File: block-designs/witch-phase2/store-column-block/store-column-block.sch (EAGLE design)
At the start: 12 parts, among them IC1 74HC125D

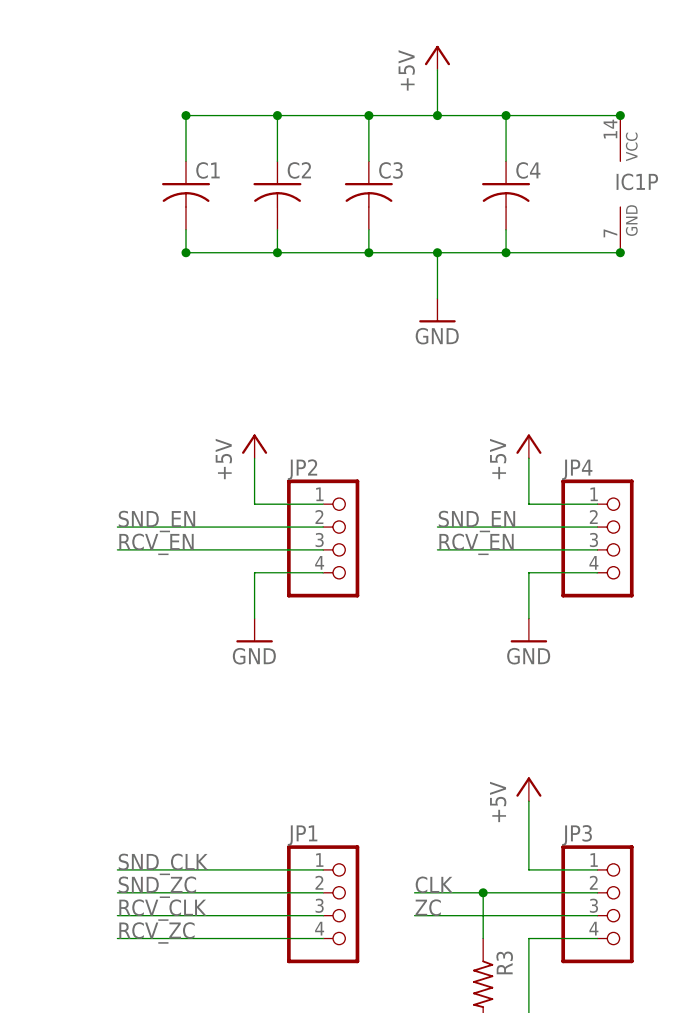
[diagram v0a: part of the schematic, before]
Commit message: updated designs for new labeling and spacing
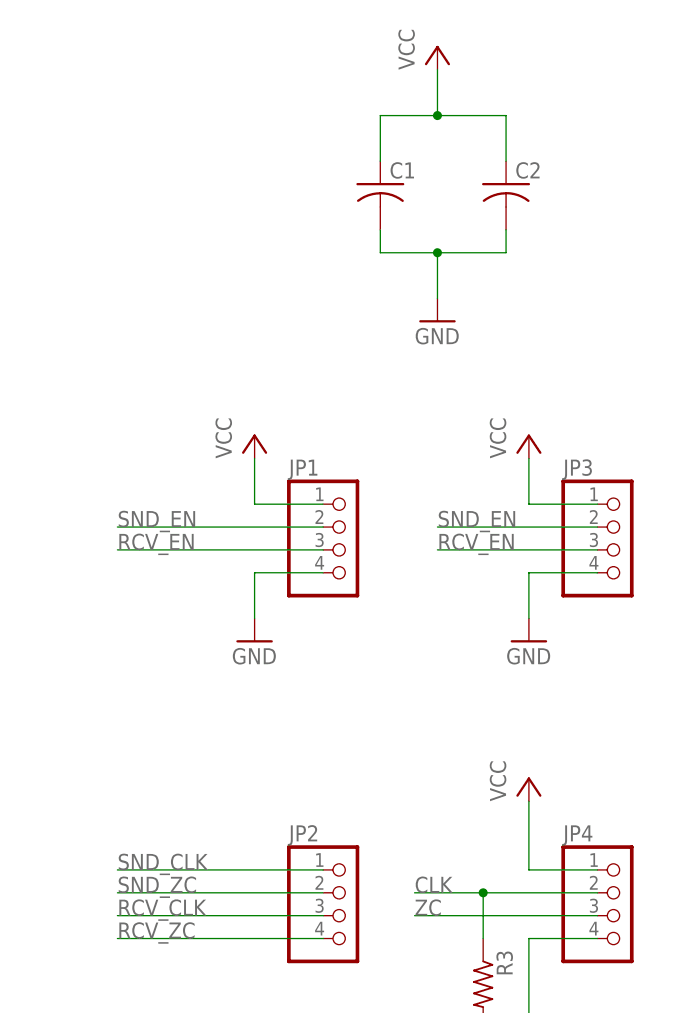
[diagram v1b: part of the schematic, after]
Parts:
- removed C3, C4: (no value), resistor:C-USC0805
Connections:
- removed net +5V: C1.1, C2.1, C3.1, C4.1, IC1P.VCC, JP2.1, JP3.1, JP4.1
- new net VCC: C1.1, C2.1, JP1.1, JP3.1, JP4.1
- net CLK: now also JP4.2; no longer JP3.2
- net GND: now also JP1.4; no longer C3.2, C4.2, IC1P.GND, JP2.4
- net RCV_CLK: now also JP2.3; no longer JP1.3
- net RCV_EN: now also JP1.3, JP3.3; no longer JP2.3, JP4.3
- net RCV_ZC: now also JP2.4; no longer JP1.4
- net SND_CLK: now also JP2.1; no longer JP1.1
- net SND_EN: now also JP1.2, JP3.2; no longer JP2.2, JP4.2
- net SND_ZC: now also JP2.2; no longer JP1.2
- net ZC: now also JP4.3; no longer JP3.3
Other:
- moved on the sheet: C1, C2, JP1, JP2, JP3, JP4

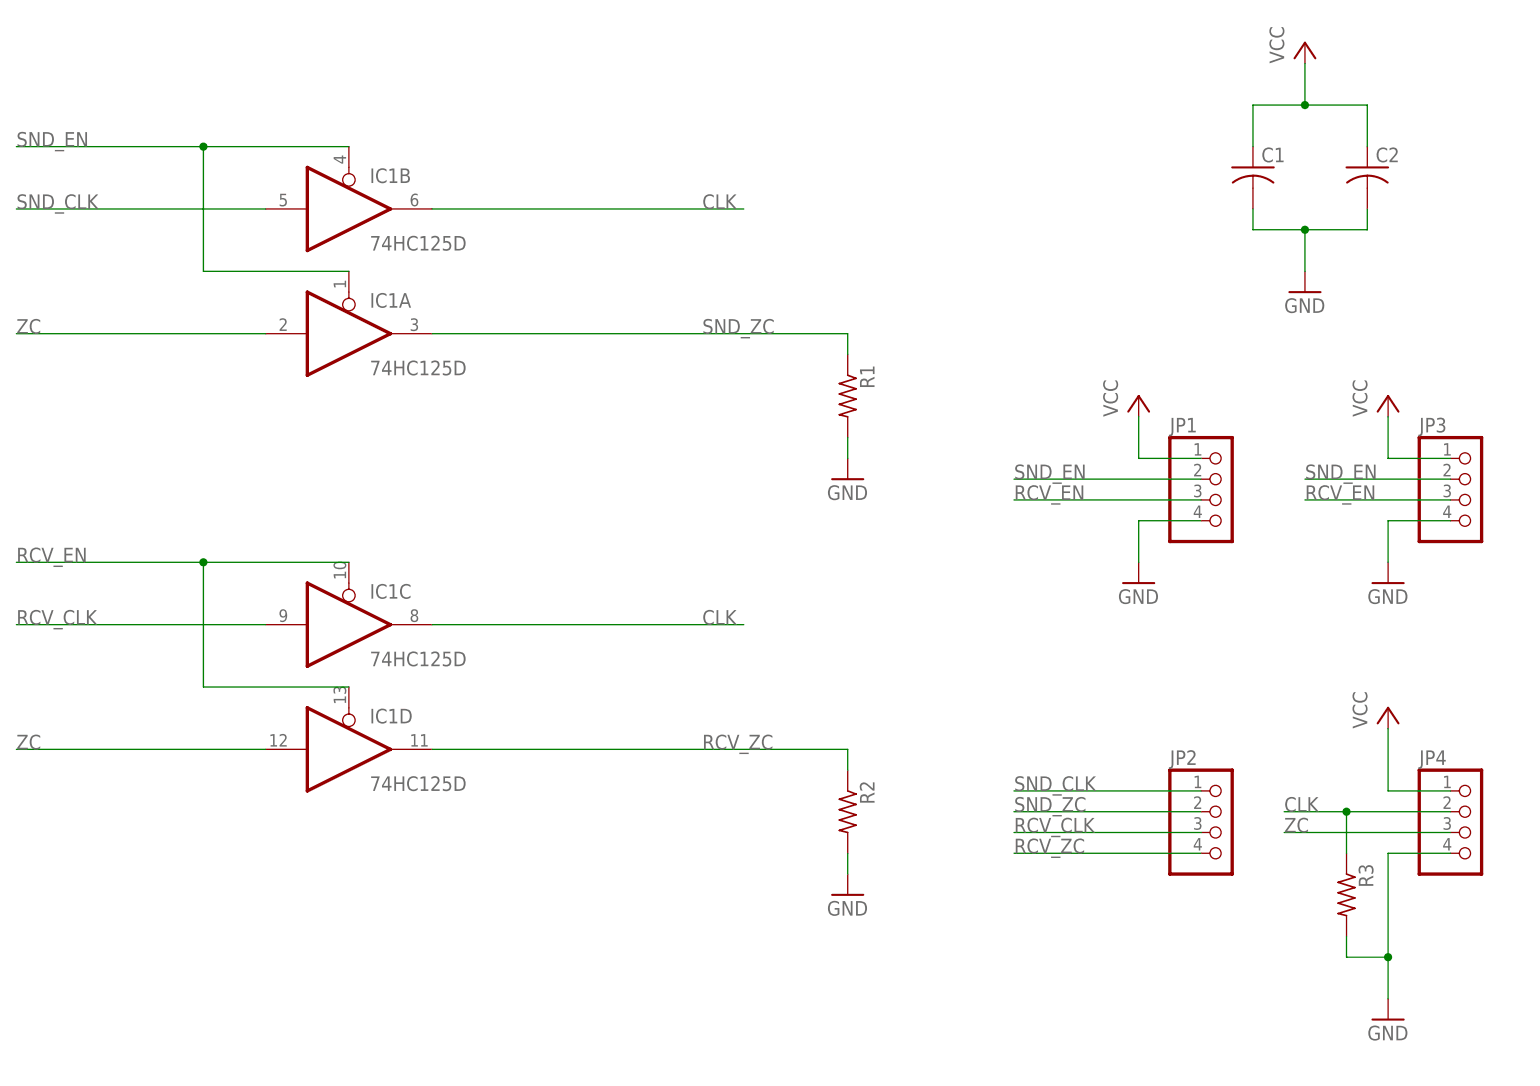
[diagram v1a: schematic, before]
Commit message: added caps on the clock lines and switch to 0603 for passives
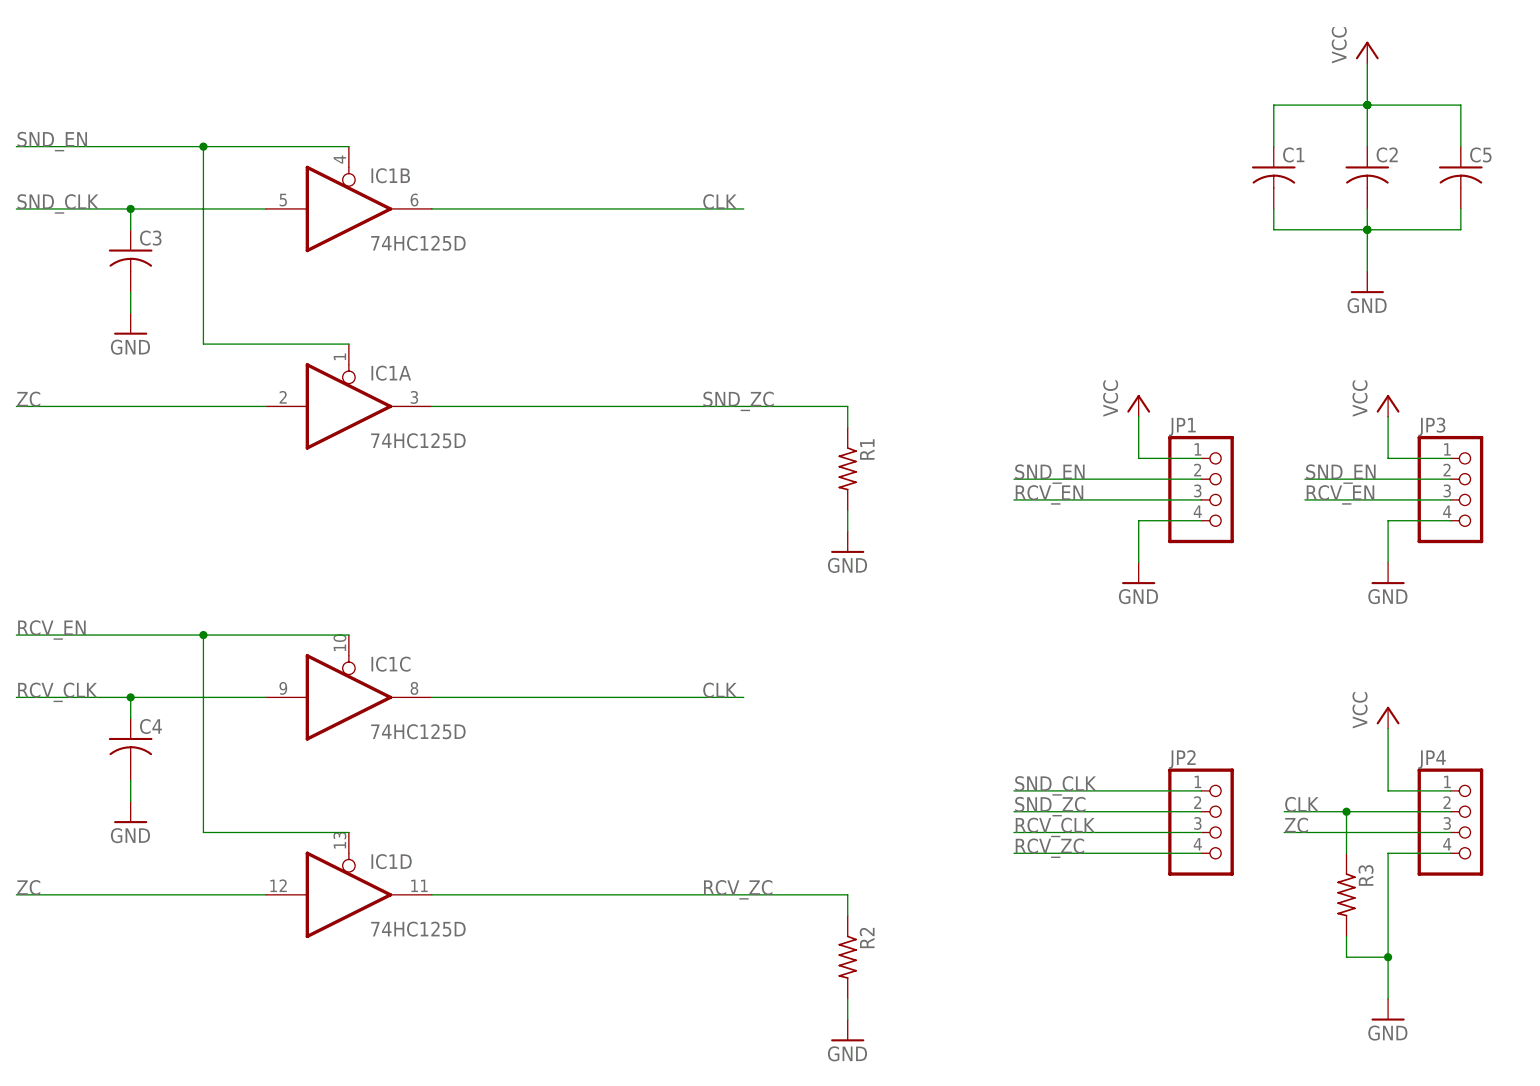
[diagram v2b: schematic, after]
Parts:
- added C3, C4, C5: (no value), resistor:C-USC0603K
- C1, C2: device resistor:C-USC0805 -> resistor:C-USC0603K
- R1, R2, R3: device resistor:R-US_R0805 -> resistor:R-US_R0603
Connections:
- net GND: now also C3.2, C4.2, C5.2
- net RCV_CLK: now also C4.1
- net SND_CLK: now also C3.1
- net VCC: now also C5.1
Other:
- moved on the sheet: C1, IC1A, IC1C, IC1D, R1, R2
